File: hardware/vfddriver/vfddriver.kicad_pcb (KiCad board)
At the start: 2 copper layers, 75 x 40 mm, 52 parts, among them J1 Connection Header, J2 HV EN, U1 IVL2-5_7, U2 LM2733YMF, U2 LM4871MX_NOPB, U3 LM2733YMF, U4 HV5812WG, U5 ATtiny412-SS

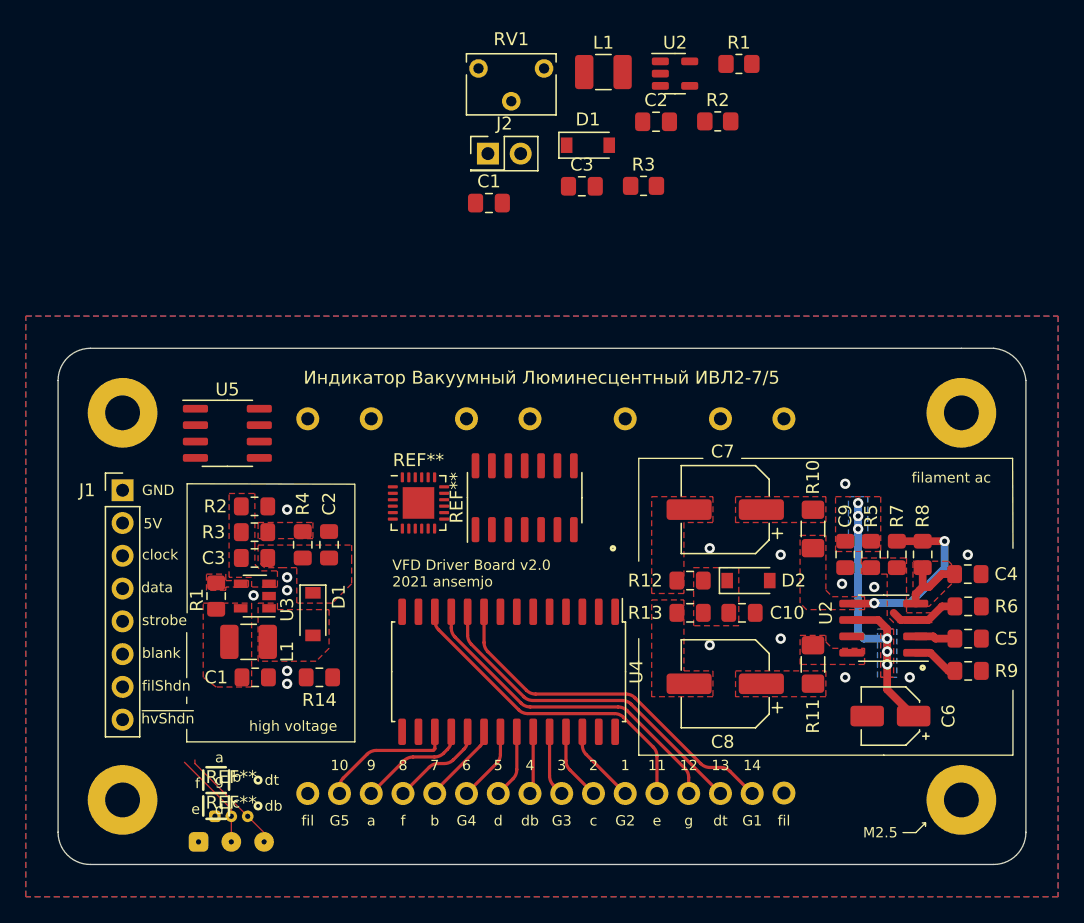
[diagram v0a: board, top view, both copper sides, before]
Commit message: hw: [WIP] begin rework vfddriver with hbridge filament
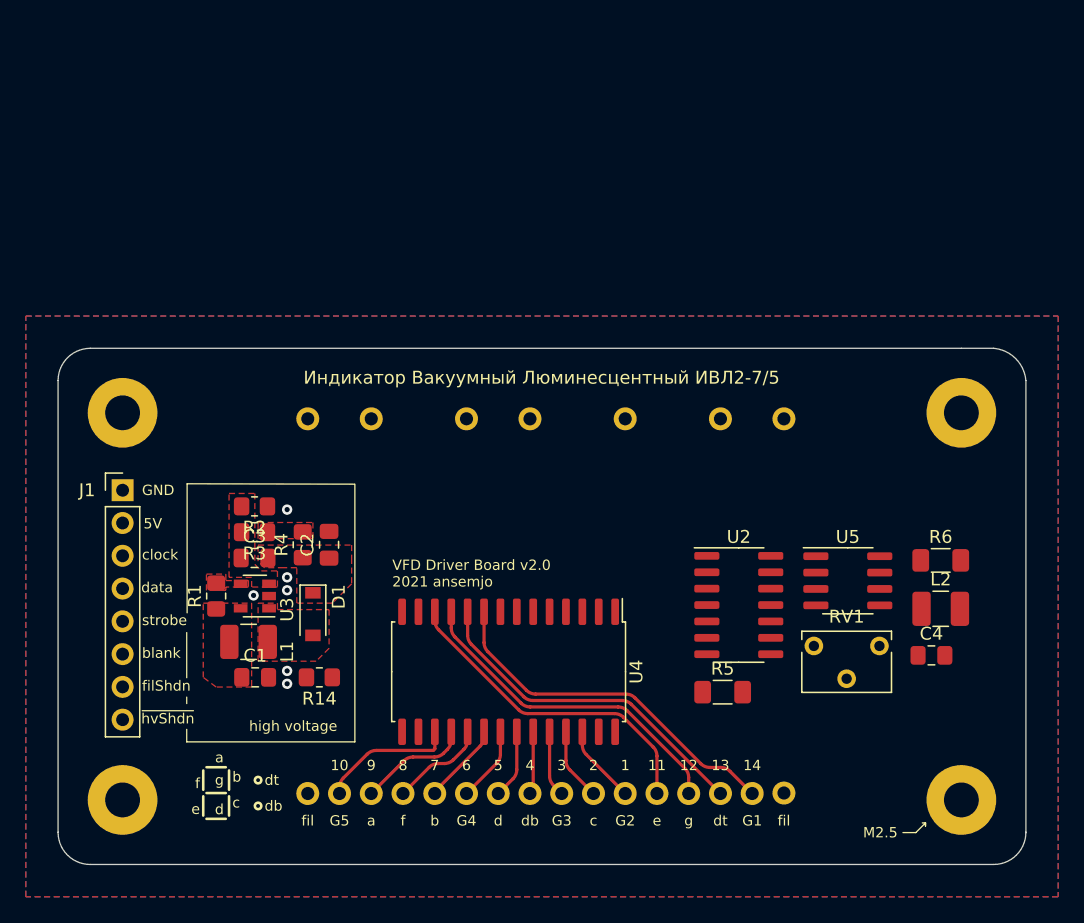
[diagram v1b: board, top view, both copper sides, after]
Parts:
- removed the C1 at (118.4, 36.2)
- removed C10, C5: 1µF, Capacitor_SMD:C_0805_2012Metric_Pad1.15x1.40mm_HandSolder
- removed the C2 at (131.3, 29.9)
- removed the C3 at (125.6, 34.9)
- removed C6: 10µF, Capacitor_SMD:CP_Elec_4x5.4
- removed C7, C8: 47µF, Capacitor_SMD:CP_Elec_6.3x5.9
- removed C9: 100nF, Capacitor_SMD:C_0805_2012Metric_Pad1.15x1.40mm_HandSolder
- removed the D1 at (126.1, 31.8)
- removed D2: 3.3V, Diode_SMD:D_SOD-123
- removed J2: HV EN, Connector_PinHeader_2.54mm:PinHeader_2x01_P2.54mm_Vertical
- removed the L1 at (127.3, 26.1)
- removed the R1 at (137.8, 25.5)
- removed R10, R11: 12Ω 0.25W, Resistor_SMD:R_1206_3216Metric_Pad1.42x1.75mm_HandSolder
- removed R12, R13: 220Ω, Resistor_SMD:R_0805_2012Metric_Pad1.15x1.40mm_HandSolder
- removed the R2 at (136.1, 29.9)
- removed the R3 at (130.4, 34.9)
- removed R7, R9: 10kΩ, Resistor_SMD:R_0805_2012Metric_Pad1.15x1.40mm_HandSolder
- removed R8: 2.2kΩ, Resistor_SMD:R_0805_2012Metric_Pad1.15x1.40mm_HandSolder
- removed REF**: UPDI_Pads_1.27, extra_libraries:UPDI_Pads_1.27
- removed REF**: VQFN-24-1EP_4x4mm_P0.5mm_EP2.45x2.45mm, Package_DFN_QFN:VQFN-24-1EP_4x4mm_P0.5mm_EP2.45x2.45mm
- removed REF**: UPDI_Pads, extra_libraries:UPDI_Pads
- removed REF**: SOIC-14_3.9x8.7mm_P1.27mm, Package_SO:SOIC-14_3.9x8.7mm_P1.27mm
- removed the U2 at (149.0, 69.2)
- removed the U2 at (132.8, 26.2)
- added L2: 10µH, Inductor_SMD:L_1210_3225Metric_Pad1.42x2.65mm_HandSolder, F.Cu at (153.4, 67.7)
- added U2: ATtiny414-SS, Package_SO:SOIC-14_3.9x8.7mm_P1.27mm, F.Cu at (137.8, 67.4)
- C1: footprint Capacitor_SMD:C_0805_2012Metric_Pad1.15x1.40mm_HandSolder -> Capacitor_SMD:C_0805_2012Metric_Pad1.18x1.45mm_HandSolder
- C2: value 4.7µF -> 82pF; footprint Capacitor_SMD:C_0805_2012Metric_Pad1.15x1.40mm_HandSolder -> Capacitor_SMD:C_0805_2012Metric_Pad1.18x1.45mm_HandSolder
- C3: value 82pF -> 4.7µF; footprint Capacitor_SMD:C_0805_2012Metric_Pad1.15x1.40mm_HandSolder -> Capacitor_SMD:C_0805_2012Metric_Pad1.18x1.45mm_HandSolder
- C4: value 10nF -> 10µF; footprint Capacitor_SMD:C_0805_2012Metric_Pad1.15x1.40mm_HandSolder -> Capacitor_SMD:C_0805_2012Metric_Pad1.18x1.45mm_HandSolder
- H1, H2, H3, H4: value MountingHole_Pad -> Mount
- J1: value Connection Header -> Header
- R1, R14: value 47kΩ -> 10kΩ; footprint Resistor_SMD:R_0805_2012Metric_Pad1.15x1.40mm_HandSolder -> Resistor_SMD:R_0805_2012Metric_Pad1.20x1.40mm_HandSolder
- R2, R3, R4: footprint Resistor_SMD:R_0805_2012Metric_Pad1.15x1.40mm_HandSolder -> Resistor_SMD:R_0805_2012Metric_Pad1.20x1.40mm_HandSolder
- R5, R6: value 10kΩ -> 0Ω; footprint Resistor_SMD:R_0805_2012Metric_Pad1.15x1.40mm_HandSolder -> Resistor_SMD:R_1206_3216Metric_Pad1.30x1.75mm_HandSolder
- RV1: value 10kΩ -> Trimmer
- U5: value ATtiny412-SS -> ZXBM5210-S
- moved RV1 51.8 mm to (148.7, 70.6)
- moved U5 49.4 mm to (146.2, 65.5)
- moved R5 15.7 mm to (136.5, 74.1), turned to 0 degrees
- moved C4 6.90 mm to (152.7, 71.3)
- moved R6 4.15 mm to (153.4, 63.9)
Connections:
- C2 pad 1: +24V -> Net-(C2-Pad1)
- C2 pad 2: GND -> HV
- C3 pad 1: Net-(C3-Pad1) -> HV
- C3 pad 2: +24V -> GND
- D1 pad 1: +24V -> HV
- R2 pad 2: Net-(C3-Pad1) -> Net-(C2-Pad1)
- R3 pad 2: Net-(C3-Pad1) -> Net-(C2-Pad1)
- R4 pad 1: +24V -> HV
- R5 pad 1: +5V -> FILAMENT-
- R6 pad 1: Net-(R5-Pad2) -> FILAMENT+
- R6 pad 2: GND -> Net-(R6-Pad2)
- RV1 pad 1: /HV -> Net-(L2-Pad1)
- RV1 pad 2: Net-(R3-Pad1) -> Net-(RV1-Pad2)
- RV1 pad 3: (no net) -> GND
- U3 pad 3: Net-(C3-Pad1) -> Net-(C2-Pad1)
- U4 pad 1: +24V -> HV
- U4 pad 2: (no net) -> unconnected-(U4-Pad2)
- U4 pad 3: (no net) -> unconnected-(U4-Pad3)
- U4 pad 4: (no net) -> unconnected-(U4-Pad4)
- U4 pad 5: (no net) -> unconnected-(U4-Pad5)
- U4 pad 6: (no net) -> unconnected-(U4-Pad6)
- U4 pad 7: (no net) -> unconnected-(U4-Pad7)
- U4 pad 8: (no net) -> unconnected-(U4-Pad8)
- U5 pad 1: +5V -> Net-(R5-Pad2)
- U5 pad 2: unconnected-(U5-Pad2) -> Net-(C4-Pad1)
- U5 pad 3: unconnected-(U5-Pad3) -> Net-(L2-Pad1)
- U5 pad 4: unconnected-(U5-Pad4) -> FIL_FWD
- U5 pad 5: unconnected-(U5-Pad5) -> FIL_REV
- U5 pad 6: UPDI -> Net-(RV1-Pad2)
- U5 pad 7: unconnected-(U5-Pad7) -> Net-(R6-Pad2)
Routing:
- net +5V: track 32.8 -> 0.00 mm, vias 6 -> 0
- net Net-(R10-Pad2): track 14.1 -> 0.00 mm, vias 2 -> 0
- net HV_DATA: track 8.57 -> 0.00 mm
- net Net-(C4-Pad1): track 5.90 -> 0.00 mm
- net Net-(R5-Pad2): track 5.42 -> 0.00 mm
- net FIL_SHDN: track 3.62 -> 0.00 mm
- net Net-(C5-Pad1): track 3.11 -> 0.00 mm
- net GND: vias 16 -> 6
- added copper zone on F.Cu, net HV
- added copper zone on F.Cu, net Net-(C2-Pad1)
- removed copper zone on F.Cu, net +24V
- removed copper zone on B.Cu, net +5V
- removed copper zone on F.Cu, net FILAMENT+
- removed copper zone on F.Cu, net FILAMENT-
- removed copper zone on F.Cu, net Net-(C10-Pad1)
- removed copper zone on F.Cu, net Net-(C3-Pad1)
- removed copper zone on F.Cu, net Net-(C4-Pad1)
- removed copper zone on F.Cu, net Net-(C7-Pad1)
- removed copper zone on F.Cu, net Net-(C8-Pad1)
- removed copper zone on F.Cu, net Net-(R10-Pad2)
- removed copper zone on F.Cu, net Net-(R11-Pad2)
- removed copper zone on F.Cu, net Net-(R5-Pad2)
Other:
- board text removed: "filament ac"

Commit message: hw: finished redesign of vfddriver frontplate
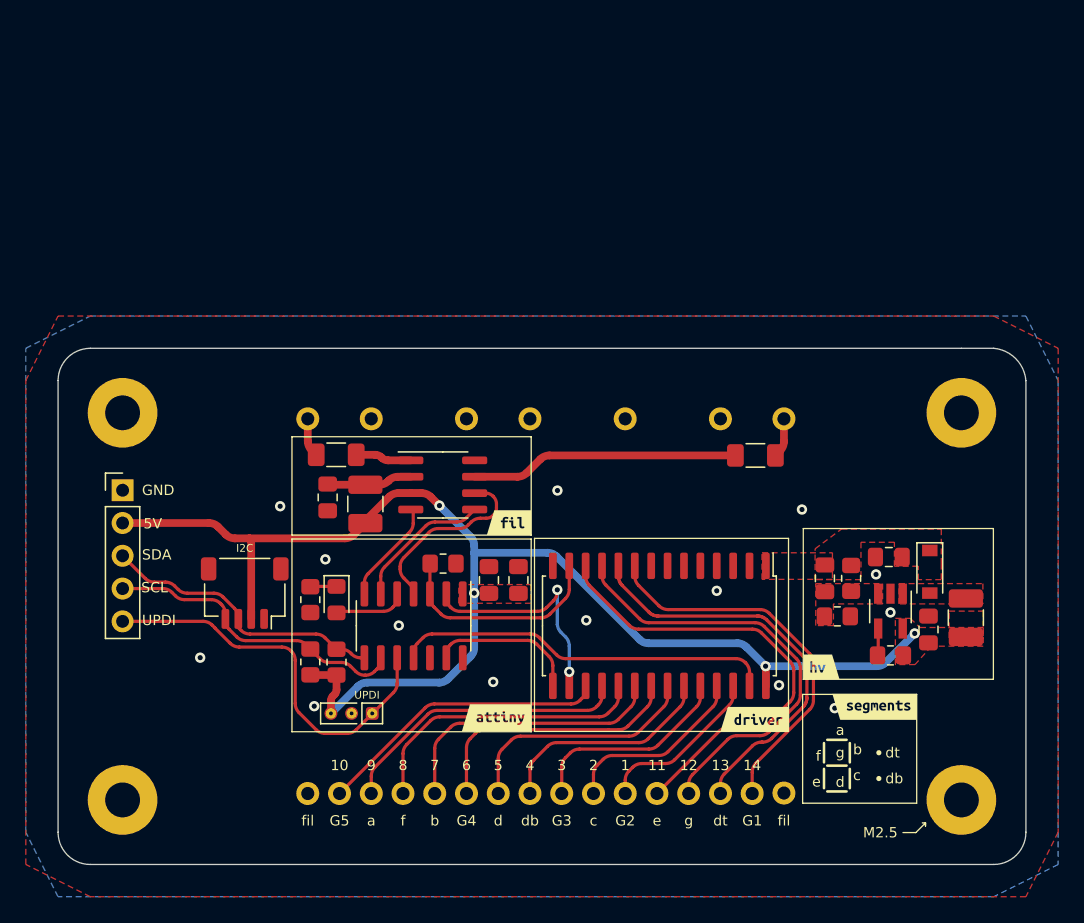
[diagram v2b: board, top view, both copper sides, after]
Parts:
- removed RV1: Trimmer, Potentiometer_THT:Potentiometer_Bourns_3266W_Vertical
- added A1: 2022, ansemjo:ahoi-mask, F.Cu at (94.2, 76.8)
- added C5: 100nF, Capacitor_SMD:C_0805_2012Metric_Pad1.18x1.45mm_HandSolder, F.Cu at (118.4, 65.5)
- added C6: 1µF, Capacitor_SMD:C_0805_2012Metric_Pad1.18x1.45mm_HandSolder, F.Cu at (120.7, 65.5)
- added D2: LED, LED_SMD:LED_0805_2012Metric_Pad1.15x1.40mm_HandSolder, F.Cu at (106.6, 67.0)
- added J2: UPDI, ansemjo:UPDI_PogoProg_pinHoles, F.Cu at (107.7, 75.8)
- added J3: I2C, Connector_JST:JST_SH_SM04B-SRSS-TB_1x04-1MP_P1.00mm_Horizontal, F.Cu at (99.5, 66.5)
- added R7: 10kΩ, Resistor_SMD:R_0805_2012Metric_Pad1.20x1.40mm_HandSolder, F.Cu at (104.5, 71.8)
- added R8: 10kΩ, Resistor_SMD:R_0805_2012Metric_Pad1.20x1.40mm_HandSolder, F.Cu at (106.6, 71.8)
- added kibuzzard-61E3696A: G***, kibuzzard-61E3696A, F.Cu at (144.2, 72.2)
- added kibuzzard-61E36996: G***, kibuzzard-61E36996, F.Cu at (119.9, 61.0)
- added kibuzzard-61E36C30: G***, kibuzzard-61E36C30, F.Cu at (119.0, 76.1)
- added kibuzzard-61E36C9E: G***, kibuzzard-61E36C9E, F.Cu at (139.0, 76.3)
- added kibuzzard-61E3771A: G***, kibuzzard-61E3771A, F.Cu at (148.3, 75.3)
- J1: footprint Connector_PinHeader_2.54mm:PinHeader_1x08_P2.54mm_Vertical -> Connector_PinHeader_2.54mm:PinHeader_1x05_P2.54mm_Vertical
- R4: value 10kΩ -> 660Ω
- U3: footprint Package_TO_SOT_SMD:SOT-23-5 -> Package_TO_SOT_SMD:SOT-23-5_HandSoldering
- moved L1 55.6 mm to (155.3, 68.4), turned to 90 degrees
- moved R1 52.5 mm to (149.5, 71.3), turned to 180 degrees
- moved C1 52.3 mm to (152.5, 69.3), turned to 90 degrees
- moved U3 49.3 mm to (149.5, 67.9), turned to -90 degrees
- moved C3 49.2 mm to (149.4, 63.7), turned to 180 degrees
- moved C4 48.4 mm to (105.9, 59.1), turned to -90 degrees
- moved D1 47.9 mm to (152.6, 64.8)
- moved R3 46.4 mm to (146.5, 65.3), turned to -90 degrees
- moved R2 46.0 mm to (145.4, 68.3)
- moved L2 45.3 mm to (108.8, 59.6), turned to 90 degrees
- moved C2 38.5 mm to (144.4, 65.3)
- moved R5 35.1 mm to (106.6, 55.8)
- moved U5 32.3 mm to (114.8, 58.1)
- moved U2 25.3 mm to (112.5, 69.0), turned to -90 degrees
- moved R6 16.5 mm to (139.0, 55.8), turned to 180 degrees
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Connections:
- J1 pad 3: IN_CLK -> SDA
- J1 pad 4: IN_DATA -> SCL
- J1 pad 5: IN_CS -> UPDI
- L2 pad 1: Net-(L2-Pad1) -> +5V
- R1 pad 2: ~{HV_SHDN} -> HV_EN
- R3 pad 1: Net-(R3-Pad1) -> HV
- R4 pad 1: HV -> Net-(D2-Pad1)
- R4 pad 2: Net-(R3-Pad1) -> GND
- U1 pad 1: FILAMENT+ -> unconnected-(U1-Pad1)
- U1 pad 16: FILAMENT- -> unconnected-(U1-Pad16)
- U2 pad 11: unconnected-(U2-Pad11) -> HV_DATA_IN
- U2 pad 13: unconnected-(U2-Pad13) -> HV_CLOCK
- U2 pad 2: unconnected-(U2-Pad2) -> HV_STROBE
- U2 pad 3: unconnected-(U2-Pad3) -> HV_BLANK
- U2 pad 4: unconnected-(U2-Pad4) -> FIL_REF
- U2 pad 5: unconnected-(U2-Pad5) -> Net-(U2-Pad5)
- U2 pad 6: unconnected-(U2-Pad6) -> FIL_REV
- U2 pad 7: unconnected-(U2-Pad7) -> FIL_FWD
- U2 pad 8: unconnected-(U2-Pad8) -> SDA
- U2 pad 9: unconnected-(U2-Pad9) -> SCL
- U3 pad 4: ~{HV_SHDN} -> HV_EN
- U4 pad 2: unconnected-(U4-Pad2) -> HV_DATA_OUT
- U4 pad 27: HV_DATA -> HV_DATA_IN
- U5 pad 3: Net-(L2-Pad1) -> +5V
- U5 pad 6: Net-(RV1-Pad2) -> FIL_REF
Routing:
- net +5V: track 0.00 -> 103.8 mm, vias 0 -> 4
- net UPDI: track 0.00 -> 30.8 mm
- net HV_DATA_IN: track 0.00 -> 29.5 mm
- net SCL: track 0.00 -> 23.9 mm
- net SDA: track 0.00 -> 22.3 mm
- net Net-(R6-Pad2): track 0.00 -> 20.8 mm
- net HV_STROBE: track 0.00 -> 18.1 mm, vias 0 -> 2
- net HV_BLANK: track 0.00 -> 17.1 mm
- net /b: track 6.32 -> 21.8 mm
- net /f: track 7.47 -> 22.8 mm
- net /G4: track 5.86 -> 20.7 mm
- net FIL_REF: track 0.00 -> 14.4 mm
- net /a: track 8.66 -> 22.9 mm
- net /d: track 5.33 -> 19.0 mm
- net /db: track 4.89 -> 17.3 mm
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- removed copper zone on F.Cu, net (none)
- removed copper zone on F.Cu, net Net-(R3-Pad1)
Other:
- board text added: "I2C"
- board text added: "SCL"
- board text added: "SDA"
- board text added: "UPDI"
- board text added: "VFD Driver Board v2.0"
- board text removed: "VFD Driver Board v2.0 2021 ansemjo"
- board text removed: "blank"
- board text removed: "clock"
- board text removed: "data"
- board text removed: "filShdn"
- board text removed: "high voltage"
- board text removed: "strobe"
- board text removed: "~{hvShdn}"
